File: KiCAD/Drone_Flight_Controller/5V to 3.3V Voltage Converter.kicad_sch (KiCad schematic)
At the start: 0 parts

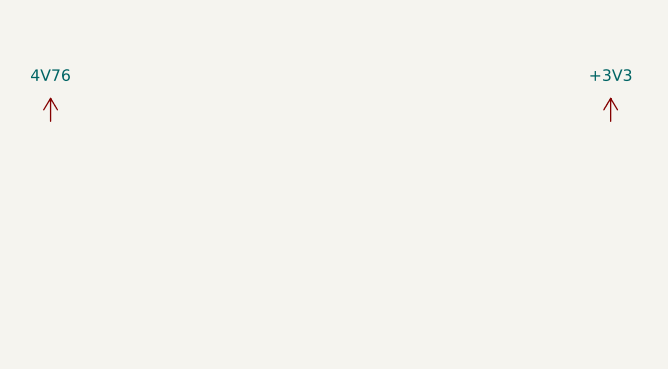
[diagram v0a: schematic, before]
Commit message: Update 5V to 3.3V Voltage Converter.kicad_sch
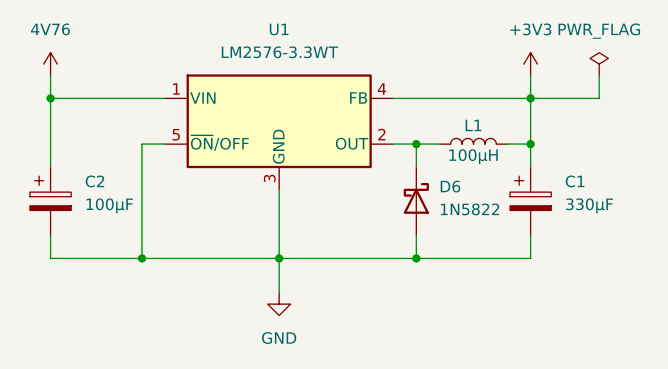
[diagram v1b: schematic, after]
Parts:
- added C1: 330µF, Capacitor_THT:CP_Radial_D6.3mm_P2.50mm, symbol Device:C_Polarized
- added C2: 100µF, Capacitor_THT:CP_Radial_D5.0mm_P2.00mm, symbol Device:C_Polarized
- added D6: 1N5822, Diode_THT:D_DO-201AD_P15.24mm_Horizontal, symbol Diode:1N5822
- added L1: 100µH, Inductor_SMD:L_1210_3225Metric_Pad1.42x2.65mm_HandSolder, symbol Device:L
- added U1: LM2576-3.3WT, Package_TO_SOT_THT:TO-220-5_Vertical, symbol Regulator_Switching:LM2576T-3.3
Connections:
- net +3V3: now also C1.1, L1.2, U1.4 (FB)
- net 4V76: now also C2.1, U1.1 (VIN)
- new net: D6.1 (K), L1.1, U1.2 (OUT)
- new net GND: C1.2, C2.2, D6.2 (A), U1.3 (GND), U1.5 (~{ON}/OFF)

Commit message: Reannotate
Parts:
- renumbered C2 to C701, C1 to C702, D6 to D701, L1 to L701, U1 to U701
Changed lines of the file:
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@@
 		(dnp no)
 		(fields_autoplaced yes)
-		(property "Reference" "C1"
+		(property "Reference" "C702"
 			(at 135.89 79.1209 0)
 			(effects
@@
 			(project ""
 				(path "/05daaa24-e506-4b9a-9564-8bf799413ca8/8391f985-3d82-4c30-aead-1780846e9311"
-					(reference "C1")
+					(reference "C702")
 					(unit 1)
 				)
@@
 		(dnp no)
 		(fields_autoplaced yes)
-		(property "Reference" "C2"
+		(property "Reference" "C701"
 			(at 82.55 79.1209 0)
 			(effects
@@
 			(project "Drone_Flight_Controller"
 				(path "/05daaa24-e506-4b9a-9564-8bf799413ca8/8391f985-3d82-4c30-aead-1780846e9311"
-					(reference "C2")
+					(reference "C701")
 					(unit 1)
 				)
@@
 		(dnp no)
 		(fields_autoplaced yes)
-		(property "Reference" "#PWR06"
+		(property "Reference" "#PWR0703"
 			(at 104.14 97.79 0)
 			(effects
@@
 			(project ""
 				(path "/05daaa24-e506-4b9a-9564-8bf799413ca8/8391f985-3d82-4c30-aead-1780846e9311"
-					(reference "#PWR06")
+					(reference "#PWR0703")
 					(unit 1)
 				)
@@
 		(dnp no)
 		(fields_autoplaced yes)
-		(property "Reference" "U1"
+		(property "Reference" "U701"
 			(at 104.14 62.23 0)
 			(effects
@@
 			(project ""
 				(path "/05daaa24-e506-4b9a-9564-8bf799413ca8/8391f985-3d82-4c30-aead-1780846e9311"
-					(reference "U1")
+					(reference "U701")
 					(unit 1)
 				)
@@
 		(dnp no)
 		(fields_autoplaced yes)
-		(property "Reference" "#PWR04"
+		(property "Reference" "#PWR0702"
 			(at 132.08 71.12 0)
 			(effects
@@
 			(project ""
 				(path "/05daaa24-e506-4b9a-9564-8bf799413ca8/8391f985-3d82-4c30-aead-1780846e9311"
-					(reference "#PWR04")
+					(reference "#PWR0702")
 					(unit 1)
 				)
@@
 		(dnp no)
 		(fields_autoplaced yes)
-		(property "Reference" "D6"
+		(property "Reference" "D701"
 			(at 121.92 79.6924 90)
 			(effects
@@
 			(project ""
 				(path "/05daaa24-e506-4b9a-9564-8bf799413ca8/8391f985-3d82-4c30-aead-1780846e9311"
-					(reference "D6")
+					(reference "D701")
 					(unit 1)
 				)
@@
 		(on_board yes)
 		(dnp no)
-		(property "Reference" "L1"
+		(property "Reference" "L701"
 			(at 125.73 72.898 90)
 			(effects
@@
 			(project ""
 				(path "/05daaa24-e506-4b9a-9564-8bf799413ca8/8391f985-3d82-4c30-aead-1780846e9311"
-					(reference "L1")
+					(reference "L701")
 					(unit 1)
 				)
@@
 		(dnp no)
 		(fields_autoplaced yes)
-		(property "Reference" "#PWR03"
+		(property "Reference" "#PWR0701"
 			(at 78.74 71.12 0)
 			(effects
@@
 			(project ""
 				(path "/05daaa24-e506-4b9a-9564-8bf799413ca8/8391f985-3d82-4c30-aead-1780846e9311"
-					(reference "#PWR03")
+					(reference "#PWR0701")
 					(unit 1)
 				)
@@
 		(dnp no)
 		(fields_autoplaced yes)
-		(property "Reference" "#FLG03"
+		(property "Reference" "#FLG0701"
 			(at 139.7 65.405 0)
 			(effects
@@
 			(project ""
 				(path "/05daaa24-e506-4b9a-9564-8bf799413ca8/8391f985-3d82-4c30-aead-1780846e9311"
-					(reference "#FLG03")
-					(unit 1)
-				)
+					(reference "#FLG0701")
+					(unit 1)
+				)

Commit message: Change to 2-sided assembly
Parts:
- U701: footprint Package_TO_SOT_THT:TO-220-5_Vertical -> Package_TO_SOT_THT:TO-220-5_Horizontal_TabDown
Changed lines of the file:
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@@
 			)
 		)
-		(property "Footprint" "Package_TO_SOT_THT:TO-220-5_Vertical"
+		(property "Footprint" "Package_TO_SOT_THT:TO-220-5_Horizontal_TabDown"
 			(at 104.14 78.74 0)
 			(effects

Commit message: Fix errors
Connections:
- net 4V76 renamed +4V76
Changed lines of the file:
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@@
 	(title_block
 		(title "5V to 3.3V Voltage Converter")
-		(date "2025-09-19")
+		(date "2025-09-21")
 		(rev "V2")
 		(company "HTL Steyr")
@@
 			)
 		)
-		(property "Value" "4V76"
+		(property "Value" "+4V76"
 			(at 78.74 62.23 0)
 			(effects

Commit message: Cleanup & Re-annotate
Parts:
- C801: renamed from C701; value 100µF -> 100µ
- C802: renamed from C702; value 330µF -> 330µ
- renumbered D701 to D801, L701 to L801, U701 to U801
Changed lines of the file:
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@@
 		(dnp no)
 		(fields_autoplaced yes)
-		(property "Reference" "C702"
+		(property "Reference" "C802"
 			(at 135.89 79.1209 0)
 			(effects
@@
 			)
 		)
-		(property "Value" "330µF"
+		(property "Value" "330µ"
 			(at 135.89 81.6609 0)
 			(effects
@@
 			(project ""
 				(path "/05daaa24-e506-4b9a-9564-8bf799413ca8/8391f985-3d82-4c30-aead-1780846e9311"
-					(reference "C702")
+					(reference "C802")
 					(unit 1)
 				)
@@
 		(dnp no)
 		(fields_autoplaced yes)
-		(property "Reference" "C701"
+		(property "Reference" "C801"
 			(at 82.55 79.1209 0)
 			(effects
@@
 			)
 		)
-		(property "Value" "100µF"
+		(property "Value" "100µ"
 			(at 82.55 81.6609 0)
 			(effects
@@
 			(project "Drone_Flight_Controller"
 				(path "/05daaa24-e506-4b9a-9564-8bf799413ca8/8391f985-3d82-4c30-aead-1780846e9311"
-					(reference "C701")
+					(reference "C801")
 					(unit 1)
 				)
@@
 		(dnp no)
 		(fields_autoplaced yes)
-		(property "Reference" "#PWR0703"
+		(property "Reference" "#PWR0802"
 			(at 104.14 97.79 0)
 			(effects
@@
 			(project ""
 				(path "/05daaa24-e506-4b9a-9564-8bf799413ca8/8391f985-3d82-4c30-aead-1780846e9311"
-					(reference "#PWR0703")
+					(reference "#PWR0802")
 					(unit 1)
 				)
@@
 		(dnp no)
 		(fields_autoplaced yes)
-		(property "Reference" "U701"
+		(property "Reference" "U801"
 			(at 104.14 62.23 0)
 			(effects
@@
 			(project ""
 				(path "/05daaa24-e506-4b9a-9564-8bf799413ca8/8391f985-3d82-4c30-aead-1780846e9311"
-					(reference "U701")
+					(reference "U801")
 					(unit 1)
 				)
@@
 		(dnp no)
 		(fields_autoplaced yes)
-		(property "Reference" "#PWR0702"
+		(property "Reference" "#PWR0803"
 			(at 132.08 71.12 0)
 			(effects
@@
 			(project ""
 				(path "/05daaa24-e506-4b9a-9564-8bf799413ca8/8391f985-3d82-4c30-aead-1780846e9311"
-					(reference "#PWR0702")
+					(reference "#PWR0803")
 					(unit 1)
 				)
@@
 		(dnp no)
 		(fields_autoplaced yes)
-		(property "Reference" "D701"
+		(property "Reference" "D801"
 			(at 121.92 79.6924 90)
 			(effects
@@
 			(project ""
 				(path "/05daaa24-e506-4b9a-9564-8bf799413ca8/8391f985-3d82-4c30-aead-1780846e9311"
-					(reference "D701")
+					(reference "D801")
 					(unit 1)
 				)
@@
 		(on_board yes)
 		(dnp no)
-		(property "Reference" "L701"
+		(property "Reference" "L801"
 			(at 125.73 72.898 90)
 			(effects
@@
 			(project ""
 				(path "/05daaa24-e506-4b9a-9564-8bf799413ca8/8391f985-3d82-4c30-aead-1780846e9311"
-					(reference "L701")
+					(reference "L801")
 					(unit 1)
 				)
@@
 		(dnp no)
 		(fields_autoplaced yes)
-		(property "Reference" "#PWR0701"
+		(property "Reference" "#PWR0801"
 			(at 78.74 71.12 0)
 			(effects
@@
 			(project ""
 				(path "/05daaa24-e506-4b9a-9564-8bf799413ca8/8391f985-3d82-4c30-aead-1780846e9311"
-					(reference "#PWR0701")
+					(reference "#PWR0801")
 					(unit 1)
 				)
@@
 		(dnp no)
 		(fields_autoplaced yes)
-		(property "Reference" "#FLG0701"
+		(property "Reference" "#FLG0801"
 			(at 139.7 65.405 0)
 			(effects
@@
 			(project ""
 				(path "/05daaa24-e506-4b9a-9564-8bf799413ca8/8391f985-3d82-4c30-aead-1780846e9311"
-					(reference "#FLG0701")
-					(unit 1)
-				)
+					(reference "#FLG0801")
+					(unit 1)
+				)
